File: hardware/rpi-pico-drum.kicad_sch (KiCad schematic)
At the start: 21 parts

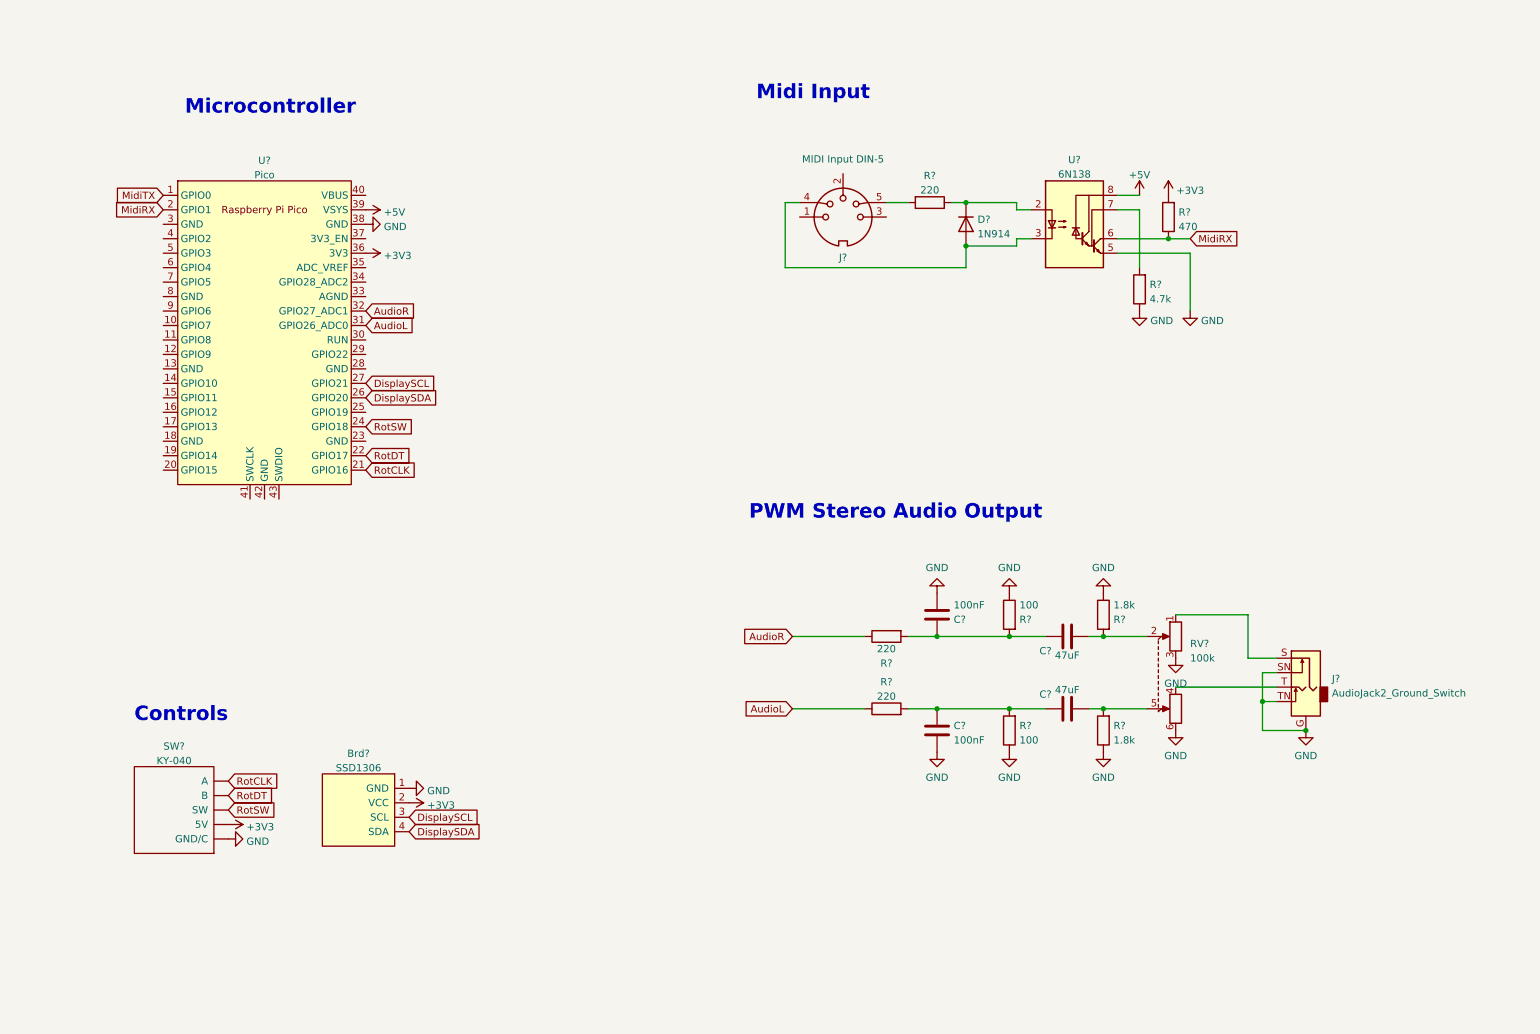
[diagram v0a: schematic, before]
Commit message: Hardware schematic updates: SD Card, I2S Audio, Power Control, and Midi Output.
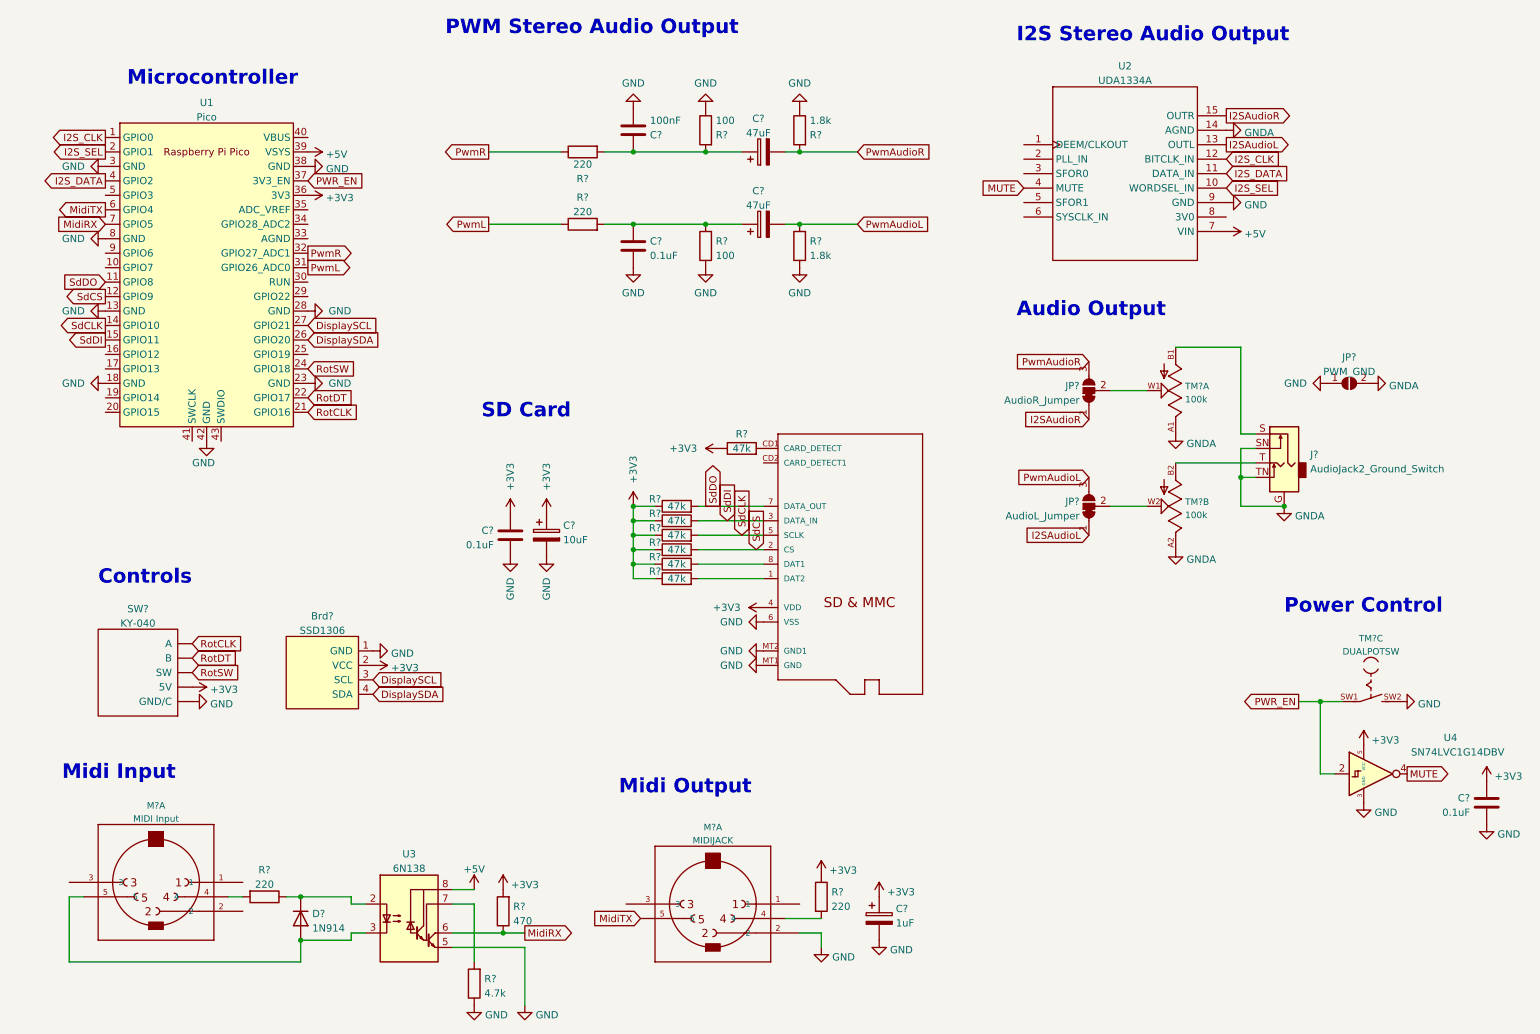
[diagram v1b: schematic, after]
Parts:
- removed C? (x2): 47uF, symbol Device:C
- removed J?: MIDI Input DIN-5, symbol Connector:DIN-5_180degree
- removed RV?: 100k, symbol Device:R_Potentiometer_Dual
- added C?: 10uF, symbol Device:C_Polarized
- added C? (x2): 47uF, symbol Device:C_Polarized
- added C? (x2): 0.1uF, symbol Device:C
- added C?: 1uF, symbol Device:C_Polarized
- added JP?: AudioR_Jumper, symbol Jumper:SolderJumper_3_Bridged12
- added JP?: AudioL_Jumper, symbol Jumper:SolderJumper_3_Bridged12
- added JP?: PWM_GND, symbol Jumper:SolderJumper_2_Open
- added M?: MICROSD, adafruit_MICROSD, symbol Adafruit:MICROSD
- added M?: MIDI Input, adafruit_CP-2350, symbol Adafruit:MIDIJACK
- added M?: MIDIJACK, adafruit_CP-2350, symbol Adafruit:MIDIJACK
- added R? (x7): 47k, symbol Device:R
- added R?: 220, symbol Device:R
- added TM? (x2): 100k, adafruit_RK0971221, symbol Adafruit:DUALPOTSW
- added TM?: DUALPOTSW, adafruit_RK0971221, symbol Adafruit:DUALPOTSW
- added U2: UDA1334A, symbol rpi-pico-drum:UDA1334A
- added U4: SN74LVC1G14DBV, Package_TO_SOT_SMD:SOT-23-5, symbol 74xGxx:SN74LVC1G14DBV
- C?: value 100nF -> 0.1uF
- gave numbers to parts that had none: 2
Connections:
- net +3V3: now also C?.1, C?.1, C?.1, C?.2, M?.4 (VDD), R?.1, R?.1, R?.1, R?.1, R?.1, R?.1, R?.1, R?.1, U4.5 (VCC)
- net +5V: now also U2.7 (VIN)
- net GND: now also U1.13 (GND), U1.18 (GND), U1.23 (GND), U1.28 (GND), U1.3 (GND), U1.42 (GND), U1.8 (GND), C?.1, C?.2, C?.2, C?.2, JP?.1 (A), M?.2, M?.6 (VSS), M?.MT1 (GND), M?.MT2 (GND1), TM?.SW2 (S), U2.9 (GND), U4.3 (GND); no longer J?.G, J?.SN, J?.TN
- net MidiRX: now also U1.7 (GPIO5); no longer U1.2 (GPIO1)
- net MidiTX: now also U1.6 (GPIO4), M?.5; no longer U1.1 (GPIO0)
- net at C?.1, R?.2, R?.2: now also C?.1 (x2)
- net PwmAudioL: now reaches R?.2
- net PwmAudioL: now also C?.2, JP?.3 (B)
- net PwmAudioR: now reaches R?.2
- net PwmAudioR: now also C?.2, JP?.3 (B)
- net at D?.2 (A), U3.3 (C2): now also M?.5
- net at R?.2: now also M?.4
- net at J?.S: now also TM?.B1 (A)
- net at J?.T: now also TM?.B2 (A)
- net SdDO: now reaches U1.11 (GPIO8)
- net SdDO: now also M?.7 (DATA_OUT), R?.2
- net SdCS: now reaches U1.12 (GPIO9)
- net SdCS: now also M?.2 (CS), R?.2
- net SdCLK: now reaches U1.14 (GPIO10)
- net SdCLK: now also M?.5 (SCLK), R?.2
- net SdDI: now reaches U1.15 (GPIO11)
- net SdDI: now also M?.3 (DATA_IN), R?.2
- net PWR_EN: now reaches U1.37 (3V3_EN)
- net PWR_EN: now also TM?.SW1 (P), U4.2
- net I2S_DATA: now reaches U1.4 (GPIO2)
- net I2S_DATA: now also U2.11 (DATA_IN)
- net AudioL renamed PwmL
- net AudioR renamed PwmR
- new net: JP?.2 (C), TM?.W2 (S)
- new net: M?.8 (DAT1), R?.2
- new net: JP?.2 (C), TM?.W1 (S)
- new net: M?.1 (DAT2), R?.2
- new net: M?.CD1 (CARD_DETECT), R?.2
- new net: M?.4, R?.2
- new net GNDA: J?.G, J?.SN, J?.TN, JP?.2 (B), TM?.A1 (E), TM?.A2 (E), U2.14 (AGND)
- new net I2SAudioL: JP?.1 (A), U2.13 (OUTL)
- new net I2SAudioR: JP?.1 (A), U2.15 (OUTR)
- new net I2S_CLK: U1.1 (GPIO0), U2.12 (BITCLK_IN)
- new net I2S_SEL: U1.2 (GPIO1), U2.10 (WORDSEL_IN)
- new net MUTE: U2.4 (MUTE), U4.4
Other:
- note added: "Audio Output"
- note added: "I2S Stereo Audio Output"
- note added: "Midi Output"
- note added: "Power Control"
- note added: "SD Card"
- moved on the sheet: Brd?, C?, D?, J?, R?, SW?, U1, U3

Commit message: Updated hardware gpio pin assignments.
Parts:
- added SW?: KY-040, symbol KY-040:KY-040
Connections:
- net +3V3: now also SW?.~ (SW)
- net GND: now also SW?.~ (SW)
- net PwmL: now also U1.21 (GPIO16); no longer U1.31 (GPIO26_ADC0)
- net PwmR: now also U1.22 (GPIO17); no longer U1.32 (GPIO27_ADC1)
- net MenuSW: now reaches U1.10 (GPIO7)
- net MenuSW: now also SW?.~ (SW)
- net MenuCLK: now reaches U1.16 (GPIO12)
- net MenuCLK: now also SW?.~ (SW)
- net MenuDT: now reaches U1.17 (GPIO13)
- net MenuDT: now also SW?.~ (SW)
- net TrellisSCL: now reaches U1.25 (GPIO19)
- net ModSW: now reaches U1.34 (GPIO28_ADC2)
- net ModSW: now also SW?.~ (SW)
- removed net RotCLK: SW?.~ (SW), U1.21 (GPIO16)
- removed net RotDT: SW?.~ (SW), U1.22 (GPIO17)
- net RotSW renamed TrellisSDA
- net TrellisSDA: no longer SW?.~ (SW)
- new net ModCLK: SW?.~ (SW), U1.31 (GPIO26_ADC0)
- new net ModDT: SW?.~ (SW), U1.32 (GPIO27_ADC1)
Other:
- moved on the sheet: Brd?, SW?
